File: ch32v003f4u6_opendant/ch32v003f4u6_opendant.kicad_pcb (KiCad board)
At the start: 2 copper layers, 20.3 x 50.4 mm, 60 parts, among them J1 USB_C_Receptacle_USB2.0, J2 BONUS, J3 BONUS, J4 PGM, J5 BATT, J6 PA1, J7 PD2, J8 VD, J9 NRST, Q1 Q_Photo_NPN, Q2 NMOS, Q3 2SC4083/L2SC4083, T1 TOUCHPAD, U1 AW32001E-POWER-PATH, U2 CH32V003F4U6, U3 SAW_FILTER_2P, U4 QMA7981, U5 XB6042Q2SV-L, U6 RS3236-3.3YUTDN4, U7 S08OB383-031

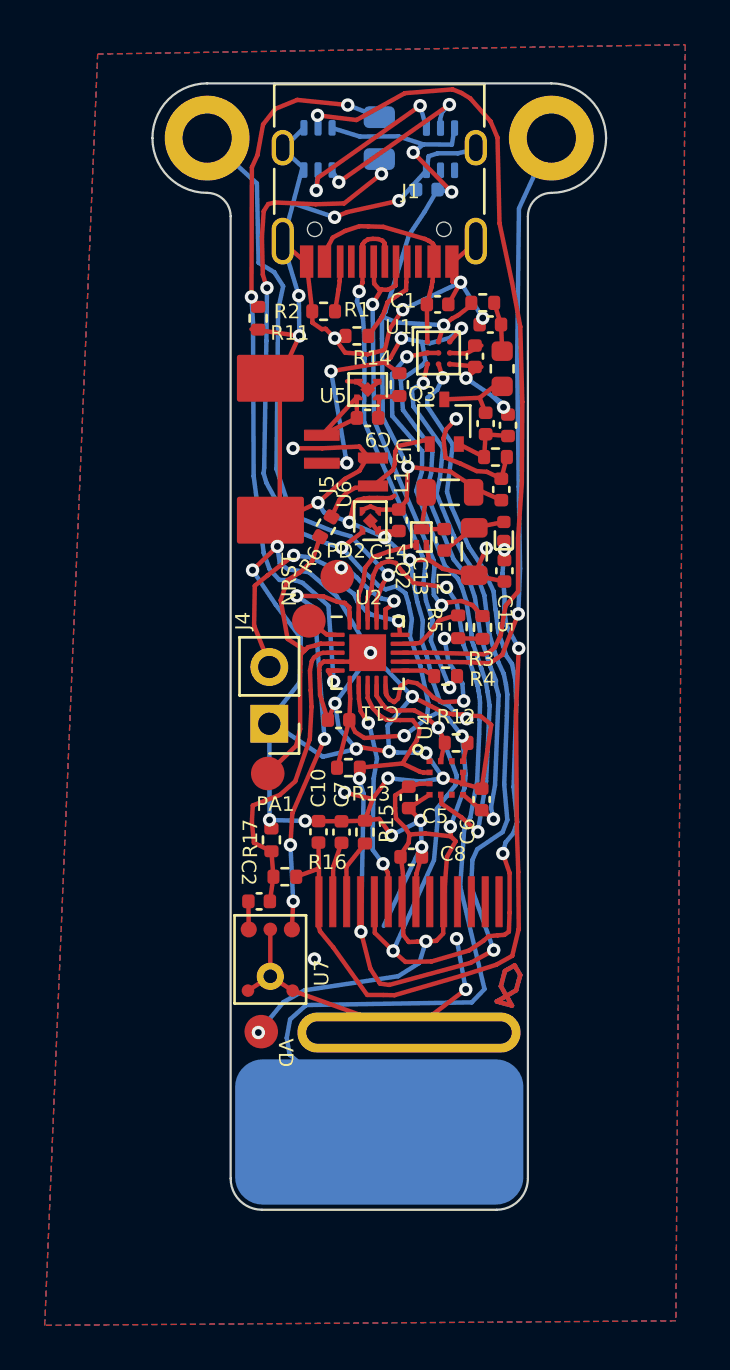
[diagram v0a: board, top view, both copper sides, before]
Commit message: Bump to what was ordered.
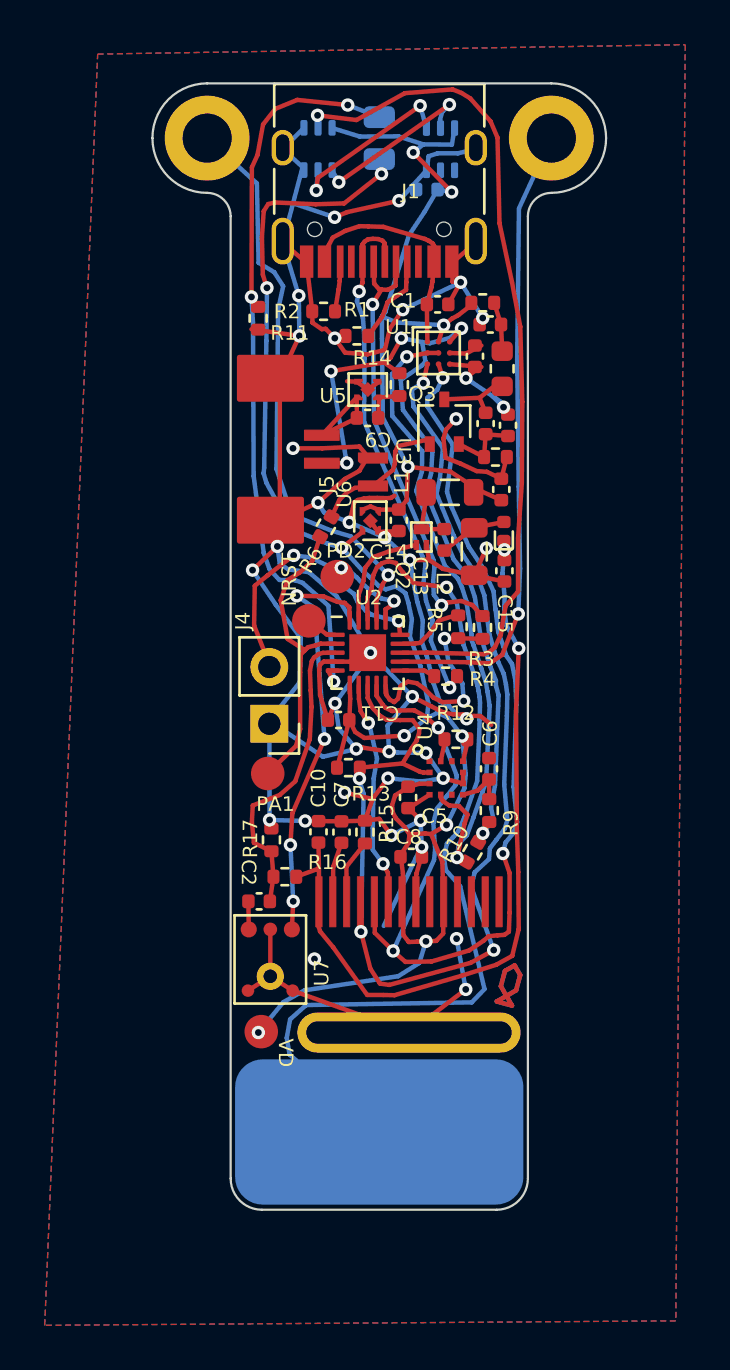
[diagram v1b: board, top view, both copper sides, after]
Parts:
- added R10: 100k, Resistor_SMD:R_0402_1005Metric, F.Cu at (102.9, 60.3)
- added R9: 0, Resistor_SMD:R_0402_1005Metric, F.Cu at (103.6, 58.4)
- moved C6 1.41 mm to (103.6, 56.6)
- moved R12 0.16 mm to (102.1, 55.2)
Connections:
- J5 pad 2: ALWYSON -> +BATT
- R14 pad 2: ALWYSON -> +BATT
- U1 pad A3: ALWYSON -> +BATT
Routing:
- net +BATT: track 0.00 -> 38.1 mm, vias 0 -> 5
- net ALWYSON: track 38.0 -> 2.27 mm, vias 5 -> 0
- net GND: track 190.6 -> 186.9 mm
- net TRIG_ON: track 26.6 -> 29.2 mm
- net TOUCH: track 40.6 -> 41.2 mm
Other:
- board text added: "cnhardware ch32v003f4u6_opendant rev-"
- board text removed: "ch32v003fun ch32v003f4u6_pendant rev -"
